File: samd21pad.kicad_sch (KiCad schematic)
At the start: 22 parts, among them J1 USB_C_Receptacle_USB2.0, J2 Conn_ARM_SWD_TagConnect_TC203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, SW1 SW_Push, SW10 SW_Push, SW2 SW_Push, SW3 SW_Push, SW4 SW_Push, SW5 SW_Push, SW6 SW_Push, SW7 SW_Push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

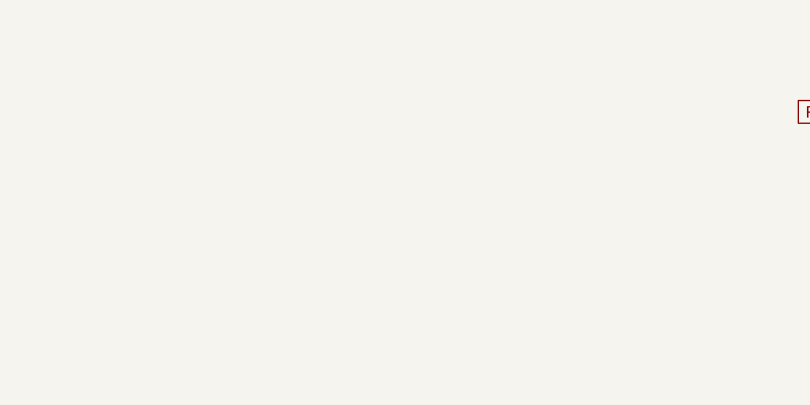
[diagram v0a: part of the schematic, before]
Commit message: 3-piece assembly edge cuts, mounting holes, plate, and silk fixes.
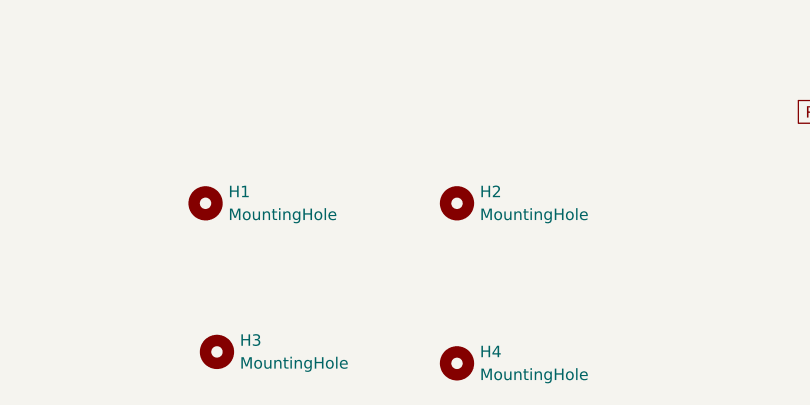
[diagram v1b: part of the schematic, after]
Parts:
- added H1, H2, H3, H4: MountingHole, samd21pad:MountingHole_M2_Pad_NonPTH_TopOnly, symbol Mechanical:MountingHole
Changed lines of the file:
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@@
+    )
+  )
+  (symbol (lib_id "Mechanical:MountingHole") (at 71.12 162.56 0) (unit 1)
+    (in_bom yes) (on_board yes) (dnp no) (fields_autoplaced)
+    (property "Reference" "H1" (at 73.66 161.29 0)
+      (effects (font (size 1.27 1.27)) (justify left))
+    )
+    (property "Value" "MountingHole" (at 73.66 163.83 0)
+      (effects (font (size 1.27 1.27)) (justify left))
+    )
+    (property "Footprint" "samd21pad:MountingHole_M2_Pad_NonPTH_TopOnly" (at 71.12 162.56 0)
+      (effects (font (size 1.27 1.27)) hide)
+    )
+    (property "Datasheet" "~" (at 71.12 162.56 0)
+      (effects (font (size 1.27 1.27)) hide)
+    )
+    (instances
+      (project "samd21pad"
+        (path "/eb5ab6b4-064a-4956-9e6e-ad6326fd260d"
+          (reference "H1") (unit 1)
+        )
+      )
     )
   )
@@
     )
   )
+  (symbol (lib_id "Mechanical:MountingHole") (at 99.06 162.56 0) (unit 1)
+    (in_bom yes) (on_board yes) (dnp no) (fields_autoplaced)
+    (property "Reference" "H2" (at 101.6 161.29 0)
+      (effects (font (size 1.27 1.27)) (justify left))
+    )
+    (property "Value" "MountingHole" (at 101.6 163.83 0)
+      (effects (font (size 1.27 1.27)) (justify left))
+    )
+    (property "Footprint" "samd21pad:MountingHole_M2_Pad_NonPTH_TopOnly" (at 99.06 162.56 0)
+      (effects (font (size 1.27 1.27)) hide)
+    )
+    (property "Datasheet" "~" (at 99.06 162.56 0)
+      (effects (font (size 1.27 1.27)) hide)
+    )
+    (instances
+      (project "samd21pad"
+        (path "/eb5ab6b4-064a-4956-9e6e-ad6326fd260d"
+          (reference "H2") (unit 1)
+        )
+      )
+    )
+  )
+  (symbol (lib_id "Mechanical:MountingHole") (at 99.06 180.34 0) (unit 1)
+    (in_bom yes) (on_board yes) (dnp no) (fields_autoplaced)
+    (property "Reference" "H4" (at 101.6 179.07 0)
+      (effects (font (size 1.27 1.27)) (justify left))
+    )
+    (property "Value" "MountingHole" (at 101.6 181.61 0)
+      (effects (font (size 1.27 1.27)) (justify left))
+    )
+    (property "Footprint" "samd21pad:MountingHole_M2_Pad_NonPTH_TopOnly" (at 99.06 180.34 0)
+      (effects (font (size 1.27 1.27)) hide)
+    )
+    (property "Datasheet" "~" (at 99.06 180.34 0)
+      (effects (font (size 1.27 1.27)) hide)
+    )
+    (instances
+      (project "samd21pad"
+        (path "/eb5ab6b4-064a-4956-9e6e-ad6326fd260d"
+          (reference "H4") (unit 1)
+        )
+      )
+    )
+  )
   (symbol (lib_id "Switch:SW_Push") (at 134.62 109.22 0) (unit 1)
     (in_bom yes) (on_board yes) (dnp no) (fields_autoplaced)
@@
         )
       )
+    )
+  )
+  (symbol (lib_id "Mechanical:MountingHole") (at 72.39 179.07 0) (unit 1)
+    (in_bom yes) (on_board yes) (dnp no) (fields_autoplaced)
+    (property "Reference" "H3" (at 74.93 177.8 0)
+      (effects (font (size 1.27 1.27)) (justify left))
+    )
+    (property "Value" "MountingHole" (at 74.93 180.34 0)
+      (effects (font (size 1.27 1.27)) (justify left))
+    )
+    (property "Footprint" "samd21pad:MountingHole_M2_Pad_NonPTH_TopOnly" (at 72.39 179.07 0)
+      (effects (font (size 1.27 1.27)) hide)
+    )
+    (property "Datasheet" "~" (at 72.39 179.07 0)
+      (effects (font (size 1.27 1.27)) hide)
+    )
+    (instances
+      (project "samd21pad"
+        (path "/eb5ab6b4-064a-4956-9e6e-ad6326fd260d"
+          (reference "H3") (unit 1)
+        )
+      )

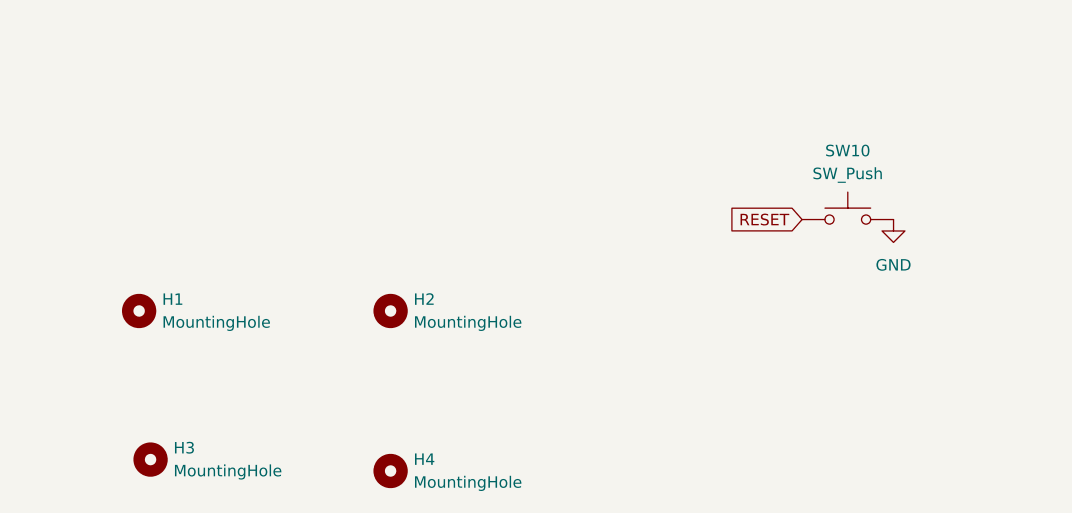
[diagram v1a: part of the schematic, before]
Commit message: BOM fixes.
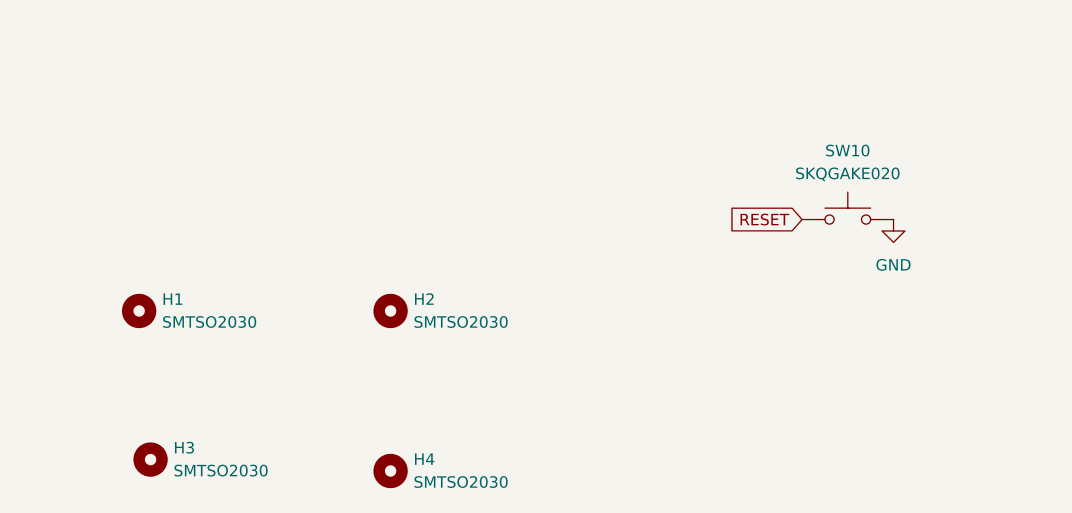
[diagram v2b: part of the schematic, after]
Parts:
- C1, C3: LCSC Part Number (none) -> C129637
- C2: LCSC Part Number (none) -> C2169363
- C4: LCSC Part Number (none) -> C129659
- H1, H2, H3, H4: value MountingHole -> SMTSO2030; LCSC Part Number (none) -> C2928170
- J1: LCSC Part Number (none) -> C3001293
- SW10: value SW_Push -> SKQGAKE020; LCSC Part Number (none) -> C388858
- U2: LCSC Part Number (none) -> C51118
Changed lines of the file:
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@@
+      (effects (font (size 1.27 1.27)) hide)
+    )
+    (property "LCSC Part Number" "C51118" (at 102.87 39.37 0)
       (effects (font (size 1.27 1.27)) hide)
     )
@@
       (effects (font (size 1.27 1.27)) (justify left))
     )
-    (property "Value" "MountingHole" (at 73.66 163.83 0)
+    (property "Value" "SMTSO2030" (at 73.66 163.83 0)
       (effects (font (size 1.27 1.27)) (justify left))
     )
@@
       (effects (font (size 1.27 1.27)) hide)
     )
+    (property "LCSC Part Number" "C2928170" (at 71.12 162.56 0)
+      (effects (font (size 1.27 1.27)) hide)
+    )
     (instances
       (project "samd21pad"
@@
       (effects (font (size 1.27 1.27)) hide)
     )
+    (property "LCSC Part Number" "" (at 134.62 96.52 0)
+      (effects (font (size 1.27 1.27)) hide)
+    )
     (pin "1")
     (pin "2")
@@
       (effects (font (size 1.27 1.27)) hide)
     )
+    (property "LCSC Part Number" "" (at 116.84 83.82 0)
+      (effects (font (size 1.27 1.27)) hide)
+    )
     (pin "1")
     (pin "2")
@@
       (effects (font (size 1.27 1.27)) hide)
     )
+    (property "LCSC Part Number" "C129659" (at 45.72 120.65 0)
+      (effects (font (size 1.27 1.27)) hide)
+    )
     (pin "1")
     (pin "2")
@@
       (effects (font (size 1.27 1.27)) hide)
     )
+    (property "LCSC Part Number" "" (at 134.62 83.82 0)
+      (effects (font (size 1.27 1.27)) hide)
+    )
     (pin "1")
     (pin "2")
@@
       (effects (font (size 1.27 1.27)) hide)
     )
+    (property "LCSC Part Number" "" (at 217.17 121.92 0)
+      (effects (font (size 1.27 1.27)) hide)
+    )
     (pin "1")
     (pin "2")
@@
     )
     (property "Datasheet" "https://www.usb.org/sites/default/files/documents/usb_type-c.zip" (at 53.34 90.17 0)
+      (effects (font (size 1.27 1.27)) hide)
+    )
+    (property "LCSC Part Number" "C3001293" (at 49.53 90.17 0)
       (effects (font (size 1.27 1.27)) hide)
     )
@@
       (effects (font (size 1.27 1.27)) hide)
     )
+    (property "LCSC Part Number" "C129637" (at 232.41 31.75 0)
+      (effects (font (size 1.27 1.27)) hide)
+    )
     (pin "1")
     (pin "2")
@@
       (effects (font (size 1.27 1.27)) (justify left))
     )
-    (property "Value" "MountingHole" (at 101.6 163.83 0)
+    (property "Value" "SMTSO2030" (at 101.6 163.83 0)
       (effects (font (size 1.27 1.27)) (justify left))
     )
@@
       (effects (font (size 1.27 1.27)) hide)
     )
+    (property "LCSC Part Number" "C2928170" (at 99.06 162.56 0)
+      (effects (font (size 1.27 1.27)) hide)
+    )
     (instances
       (project "samd21pad"
@@
       (effects (font (size 1.27 1.27)) (justify left))
     )
-    (property "Value" "MountingHole" (at 101.6 181.61 0)
+    (property "Value" "SMTSO2030" (at 101.6 181.61 0)
       (effects (font (size 1.27 1.27)) (justify left))
     )
@@
       (effects (font (size 1.27 1.27)) hide)
     )
+    (property "LCSC Part Number" "C2928170" (at 99.06 180.34 0)
+      (effects (font (size 1.27 1.27)) hide)
+    )
     (instances
       (project "samd21pad"
@@
     )
     (property "Datasheet" "~" (at 134.62 104.14 0)
+      (effects (font (size 1.27 1.27)) hide)
+    )
+    (property "LCSC Part Number" "" (at 134.62 109.22 0)
       (effects (font (size 1.27 1.27)) hide)
     )
@@
       (effects (font (size 1.27 1.27)) hide)
     )
+    (property "LCSC Part Number" "" (at 172.72 38.1 0)
+      (effects (font (size 1.27 1.27)) hide)
+    )
     (pin "1")
     (pin "2")
@@
       (effects (font (size 1.27 1.27)) hide)
     )
+    (property "LCSC Part Number" "" (at 116.84 109.22 0)
+      (effects (font (size 1.27 1.27)) hide)
+    )
     (pin "1")
     (pin "2")
@@
       (effects (font (size 1.27 1.27)) hide)
     )
+    (property "LCSC Part Number" "" (at 80.01 82.55 0)
+      (effects (font (size 1.27 1.27)) hide)
+    )
     (pin "1")
     (pin "2")
@@
       (effects (font (size 1.27 1.27)) hide)
     )
+    (property "LCSC Part Number" "" (at 80.01 80.01 0)
+      (effects (font (size 1.27 1.27)) hide)
+    )
     (pin "1")
     (pin "2")
@@
       (effects (font (size 1.27 1.27)) hide)
     )
+    (property "LCSC Part Number" "C2169363" (at 242.57 31.75 0)
+      (effects (font (size 1.27 1.27)) hide)
+    )
     (pin "1")
     (pin "2")
@@
       (effects (font (size 1.27 1.27)) hide)
     )
+    (property "LCSC Part Number" "" (at 152.4 83.82 0)
+      (effects (font (size 1.27 1.27)) hide)
+    )
     (pin "1")
     (pin "2")
@@
       (effects (font (size 1.27 1.27)) hide)
     )
+    (property "LCSC Part Number" "C129637" (at 113.03 39.37 0)
+      (effects (font (size 1.27 1.27)) hide)
+    )
     (pin "1")
     (pin "2")
@@
       (effects (font (size 1.27 1.27)) hide)
     )
+    (property "LCSC Part Number" "" (at 45.72 128.27 0)
+      (effects (font (size 1.27 1.27)) hide)
+    )
     (pin "1")
     (pin "2")
@@
       (effects (font (size 1.27 1.27)) hide)
     )
+    (property "LCSC Part Number" "" (at 116.84 96.52 0)
+      (effects (font (size 1.27 1.27)) hide)
+    )
     (pin "1")
     (pin "2")
@@
       (effects (font (size 1.27 1.27)) hide)
     )
+    (property "LCSC Part Number" "" (at 152.4 109.22 0)
+      (effects (font (size 1.27 1.27)) hide)
+    )
     (pin "1")
     (pin "2")
@@
       (effects (font (size 1.27 1.27)) hide)
     )
+    (property "LCSC Part Number" "" (at 152.4 96.52 0)
+      (effects (font (size 1.27 1.27)) hide)
+    )
     (pin "1")
     (pin "2")
@@
       (effects (font (size 1.27 1.27)) (justify left))
     )
-    (property "Value" "MountingHole" (at 74.93 180.34 0)
+    (property "Value" "SMTSO2030" (at 74.93 180.34 0)
       (effects (font (size 1.27 1.27)) (justify left))
     )
@@
       (effects (font (size 1.27 1.27)) hide)
     )
+    (property "LCSC Part Number" "C2928170" (at 72.39 179.07 0)
+      (effects (font (size 1.27 1.27)) hide)
+    )
     (instances
       (project "samd21pad"
@@
       (effects (font (size 1.27 1.27)))
     )
-    (property "Value" "SW_Push" (at 149.86 147.32 0)
+    (property "Value" "SKQGAKE020" (at 149.86 147.32 0)
       (effects (font (size 1.27 1.27)))
     )
@@
       (effects (font (size 1.27 1.27)) hide)
     )
+    (property "LCSC Part Number" "C388858" (at 149.86 152.4 0)
+      (effects (font (size 1.27 1.27)) hide)
+    )
     (pin "1")
     (pin "2")
@@
       (effects (font (size 1.27 1.27)) hide)
     )
+    (property "LCSC Part Number" "" (at 242.57 88.9 0)
+      (effects (font (size 1.27 1.27)) hide)
+    )

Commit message: Add silk for the bottom plate for the SMK meetup.
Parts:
- SW10: MPN (none) -> SKQGAKE020
- U1: MPN (none) -> ATSAMD21E17D-A
- U2: MPN (none) -> AP2112K-3.3
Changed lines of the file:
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@@
+      (effects (font (size 1.27 1.27)) hide)
+    )
+    (property "MPN" "AP2112K-3.3" (at 102.87 39.37 0)
       (effects (font (size 1.27 1.27)) hide)
     )
@@
       (effects (font (size 1.27 1.27)) hide)
     )
+    (property "MPN" "" (at 71.12 162.56 0)
+      (effects (font (size 1.27 1.27)) hide)
+    )
     (instances
       (project "samd21pad"
@@
       (effects (font (size 1.27 1.27)) hide)
     )
+    (property "MPN" "" (at 134.62 96.52 0)
+      (effects (font (size 1.27 1.27)) hide)
+    )
     (pin "1")
     (pin "2")
@@
       (effects (font (size 1.27 1.27)) hide)
     )
+    (property "MPN" "" (at 116.84 83.82 0)
+      (effects (font (size 1.27 1.27)) hide)
+    )
     (pin "1")
     (pin "2")
@@
       (effects (font (size 1.27 1.27)) hide)
     )
+    (property "MPN" "" (at 45.72 120.65 0)
+      (effects (font (size 1.27 1.27)) hide)
+    )
     (pin "1")
     (pin "2")
@@
       (effects (font (size 1.27 1.27)) hide)
     )
+    (property "MPN" "" (at 134.62 83.82 0)
+      (effects (font (size 1.27 1.27)) hide)
+    )
     (pin "1")
     (pin "2")
@@
       (effects (font (size 1.27 1.27)) hide)
     )
+    (property "MPN" "" (at 217.17 121.92 0)
+      (effects (font (size 1.27 1.27)) hide)
+    )
     (pin "1")
     (pin "2")
@@
     )
     (property "LCSC Part Number" "C3001293" (at 49.53 90.17 0)
+      (effects (font (size 1.27 1.27)) hide)
+    )
+    (property "MPN" "" (at 49.53 90.17 0)
       (effects (font (size 1.27 1.27)) hide)
     )
@@
       (effects (font (size 1.27 1.27)) hide)
     )
+    (property "MPN" "" (at 232.41 31.75 0)
+      (effects (font (size 1.27 1.27)) hide)
+    )
     (pin "1")
     (pin "2")
@@
       (effects (font (size 1.27 1.27)) hide)
     )
+    (property "MPN" "" (at 99.06 162.56 0)
+      (effects (font (size 1.27 1.27)) hide)
+    )
     (instances
       (project "samd21pad"
@@
       (effects (font (size 1.27 1.27)) hide)
     )
+    (property "MPN" "" (at 99.06 180.34 0)
+      (effects (font (size 1.27 1.27)) hide)
+    )
     (instances
       (project "samd21pad"
@@
     )
     (property "LCSC Part Number" "" (at 134.62 109.22 0)
+      (effects (font (size 1.27 1.27)) hide)
+    )
+    (property "MPN" "" (at 134.62 109.22 0)
       (effects (font (size 1.27 1.27)) hide)
     )
@@
       (effects (font (size 1.27 1.27)) hide)
     )
+    (property "MPN" "" (at 172.72 38.1 0)
+      (effects (font (size 1.27 1.27)) hide)
+    )
     (pin "1")
     (pin "2")
@@
       (effects (font (size 1.27 1.27)) hide)
     )
+    (property "MPN" "" (at 116.84 109.22 0)
+      (effects (font (size 1.27 1.27)) hide)
+    )
     (pin "1")
     (pin "2")
@@
       (effects (font (size 1.27 1.27)) hide)
     )
+    (property "MPN" "" (at 80.01 82.55 0)
+      (effects (font (size 1.27 1.27)) hide)
+    )
     (pin "1")
     (pin "2")
@@
       (effects (font (size 1.27 1.27)) hide)
     )
+    (property "MPN" "" (at 80.01 80.01 0)
+      (effects (font (size 1.27 1.27)) hide)
+    )
     (pin "1")
     (pin "2")
@@
       (effects (font (size 1.27 1.27)) hide)
     )
+    (property "MPN" "" (at 242.57 31.75 0)
+      (effects (font (size 1.27 1.27)) hide)
+    )
     (pin "1")
     (pin "2")
@@
       (effects (font (size 1.27 1.27)) hide)
     )
+    (property "MPN" "" (at 152.4 83.82 0)
+      (effects (font (size 1.27 1.27)) hide)
+    )
     (pin "1")
     (pin "2")
@@
       (effects (font (size 1.27 1.27)) hide)
     )
+    (property "MPN" "" (at 113.03 39.37 0)
+      (effects (font (size 1.27 1.27)) hide)
+    )
     (pin "1")
     (pin "2")
@@
       (effects (font (size 1.27 1.27)) hide)
     )
+    (property "MPN" "" (at 45.72 128.27 0)
+      (effects (font (size 1.27 1.27)) hide)
+    )
     (pin "1")
     (pin "2")
@@
       (effects (font (size 1.27 1.27)) hide)
     )
+    (property "MPN" "" (at 116.84 96.52 0)
+      (effects (font (size 1.27 1.27)) hide)
+    )
     (pin "1")
     (pin "2")
@@
       (effects (font (size 1.27 1.27)) hide)
     )
+    (property "MPN" "" (at 152.4 109.22 0)
+      (effects (font (size 1.27 1.27)) hide)
+    )
     (pin "1")
     (pin "2")
@@
       (effects (font (size 1.27 1.27)) hide)
     )
+    (property "MPN" "" (at 152.4 96.52 0)
+      (effects (font (size 1.27 1.27)) hide)
+    )
     (pin "1")
     (pin "2")
@@
       (effects (font (size 1.27 1.27)) hide)
     )
+    (property "MPN" "" (at 72.39 179.07 0)
+      (effects (font (size 1.27 1.27)) hide)
+    )
     (instances
       (project "samd21pad"
@@
       (effects (font (size 1.27 1.27)) hide)
     )
+    (property "MPN" "SKQGAKE020" (at 149.86 152.4 0)
+      (effects (font (size 1.27 1.27)) hide)
+    )
     (pin "1")
     (pin "2")
@@
       (effects (font (size 1.27 1.27)) hide)
     )
+    (property "MPN" "ATSAMD21E17D-A" (at 242.57 88.9 0)
+      (effects (font (size 1.27 1.27)) hide)
+    )
